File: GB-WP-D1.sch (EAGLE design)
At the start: 9 parts

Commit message: Add files via upload
WEMOS D1 mini size
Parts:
- removed JP2: (no value), pinhead_v2:PINHD-1X5/OCT
- removed JP5: (no value), pinhead_v2:PINHD-1X4/OCT
- added U$3: KAMENRIDER_LOGOV2_COLOR_OPAC, kamenrider:KAMENRIDER_LOGOV2_COLOR_OPAC
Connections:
- net 3.3V: no longer JP2.5, JP5.3
- net 5V: no longer JP2.4
- net D0: no longer JP2.1
- net D2: no longer JP5.1
- net D3: no longer JP2.2
- net GND: no longer JP2.3, JP5.4
- net N$7: no longer JP5.2
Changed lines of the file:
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@@
 <part name="JP4" library="pinhead_v2" deviceset="PINHD-1X6" device="/OCT"/>
 <part name="JP1" library="pinhead_v2" deviceset="PINHD-1X4" device="/OCT"/>
-<part name="JP5" library="pinhead_v2" deviceset="PINHD-1X4" device="/OCT"/>
 <part name="LED1" library="led" library_urn="urn:adsk.eagle:library:259" deviceset="LED" device="3MM" package3d_urn="urn:adsk.eagle:package:15797/1"/>
-<part name="JP2" library="pinhead_v2" deviceset="PINHD-1X5" device="/OCT"/>
 <part name="JP3" library="pinhead_v2" deviceset="PINHD-1X8" device="/OCT"/>
 <part name="JP6" library="pinhead_v2" deviceset="PINHD-1X8" device="/OCT"/>
+<part name="U$3" library="kamenrider" deviceset="KAMENRIDER_LOGO" device="V2_COLOR_OPAC"/>
 </parts>
 <sheets>
@@
 <attribute name="VALUE" x="153.67" y="55.88" size="1.778" layer="96"/>
 </instance>
-<instance part="JP5" gate="A" x="167.64" y="63.5" smashed="yes">
-<attribute name="NAME" x="161.29" y="71.755" size="1.778" layer="95"/>
-<attribute name="VALUE" x="161.29" y="55.88" size="1.778" layer="96"/>
-</instance>
 <instance part="LED1" gate="G$1" x="109.22" y="88.9" smashed="yes">
 <attribute name="NAME" x="112.776" y="84.328" size="1.778" layer="95" rot="R90"/>
 <attribute name="VALUE" x="114.935" y="84.328" size="1.778" layer="96" rot="R90"/>
 </instance>
-<instance part="JP2" gate="A" x="96.52" y="73.66" smashed="yes">
-<attribute name="NAME" x="90.17" y="81.915" size="1.778" layer="95"/>
-<attribute name="VALUE" x="90.17" y="63.5" size="1.778" layer="96"/>
-</instance>
 <instance part="JP3" gate="A" x="31.242" y="101.6" smashed="yes" rot="MR0">
 <attribute name="VALUE" x="47.752" y="86.36" size="1.778" layer="96" rot="MR0"/>
@@
 <attribute name="VALUE" x="227.33" y="88.9" size="1.778" layer="96" rot="MR0"/>
 </instance>
+<instance part="U$3" gate="G$1" x="86.36" y="7.62" smashed="yes"/>
 </instances>
 <busses>
@@
 <junction x="205.74" y="96.52"/>
 <wire x1="193.04" y1="96.52" x2="193.04" y2="60.96" width="0.1524" layer="91"/>
-<pinref part="JP5" gate="A" pin="4"/>
-<wire x1="193.04" y1="60.96" x2="165.1" y2="60.96" width="0.1524" layer="91"/>
+<wire x1="193.04" y1="60.96" x2="157.48" y2="60.96" width="0.1524" layer="91"/>
 <pinref part="JP1" gate="A" pin="4"/>
-<wire x1="157.48" y1="60.96" x2="165.1" y2="60.96" width="0.1524" layer="91"/>
 <pinref part="U$2" gate="G$1" pin="GND"/>
 <pinref part="JP4" gate="A" pin="6"/>
@@
 <wire x1="180.34" y1="78.74" x2="101.6" y2="78.74" width="0.1524" layer="91"/>
 <pinref part="JP6" gate="A" pin="7"/>
-<junction x="165.1" y="60.96"/>
 <wire x1="101.6" y1="78.74" x2="101.6" y2="73.66" width="0.1524" layer="91"/>
-<pinref part="JP2" gate="A" pin="3"/>
 <wire x1="101.6" y1="73.66" x2="93.98" y2="73.66" width="0.1524" layer="91"/>
 </segment>
@@
 <wire x1="223.52" y1="104.14" x2="187.96" y2="104.14" width="0.1524" layer="91"/>
 <wire x1="187.96" y1="104.14" x2="187.96" y2="68.58" width="0.1524" layer="91"/>
-<pinref part="JP5" gate="A" pin="1"/>
-<wire x1="187.96" y1="68.58" x2="165.1" y2="68.58" width="0.1524" layer="91"/>
+<wire x1="187.96" y1="68.58" x2="157.48" y2="68.58" width="0.1524" layer="91"/>
 <pinref part="JP1" gate="A" pin="1"/>
-<wire x1="165.1" y1="68.58" x2="157.48" y2="68.58" width="0.1524" layer="91"/>
 <pinref part="JP6" gate="A" pin="4"/>
-<junction x="165.1" y="68.58"/>
 </segment>
 </net>
@@
 <segment>
 <label x="40.64" y="106.68" size="1.778" layer="95"/>
-<pinref part="JP2" gate="A" pin="1"/>
-<wire x1="39.37" y1="106.68" x2="40.64" y2="106.68" width="0.1524" layer="91"/>
-<wire x1="40.64" y1="106.68" x2="93.98" y2="106.68" width="0.1524" layer="91"/>
+<wire x1="33.782" y1="106.68" x2="93.98" y2="106.68" width="0.1524" layer="91"/>
 <wire x1="93.98" y1="106.68" x2="93.98" y2="78.74" width="0.1524" layer="91"/>
 <pinref part="JP3" gate="A" pin="3"/>
-<wire x1="33.782" y1="106.68" x2="39.37" y2="106.68" width="0.1524" layer="91"/>
 </segment>
 </net>
@@
 <wire x1="223.52" y1="101.6" x2="182.88" y2="101.6" width="0.1524" layer="91"/>
 <wire x1="182.88" y1="101.6" x2="182.88" y2="76.2" width="0.1524" layer="91"/>
-<pinref part="JP2" gate="A" pin="2"/>
 <wire x1="182.88" y1="76.2" x2="93.98" y2="76.2" width="0.1524" layer="91"/>
 <pinref part="JP6" gate="A" pin="5"/>
@@
 <wire x1="215.9" y1="53.34" x2="99.06" y2="53.34" width="0.1524" layer="91"/>
 <wire x1="99.06" y1="53.34" x2="99.06" y2="71.12" width="0.1524" layer="91"/>
-<pinref part="JP2" gate="A" pin="4"/>
 <wire x1="99.06" y1="71.12" x2="93.98" y2="71.12" width="0.1524" layer="91"/>
 <pinref part="JP6" gate="A" pin="8"/>
@@
 <wire x1="127" y1="91.44" x2="172.72" y2="91.44" width="0.1524" layer="91"/>
 <wire x1="172.72" y1="91.44" x2="172.72" y2="63.5" width="0.1524" layer="91"/>
-<pinref part="JP5" gate="A" pin="3"/>
 <pinref part="JP1" gate="A" pin="3"/>
-<wire x1="157.48" y1="63.5" x2="165.1" y2="63.5" width="0.1524" layer="91"/>
-<wire x1="172.72" y1="63.5" x2="165.1" y2="63.5" width="0.1524" layer="91"/>
-<junction x="165.1" y="63.5"/>
-<pinref part="JP2" gate="A" pin="5"/>
+<wire x1="172.72" y1="63.5" x2="157.48" y2="63.5" width="0.1524" layer="91"/>
 <wire x1="53.34" y1="68.58" x2="93.98" y2="68.58" width="0.1524" layer="91"/>
 </segment>
@@
 <wire x1="223.52" y1="106.68" x2="185.42" y2="106.68" width="0.1524" layer="91"/>
 <wire x1="185.42" y1="106.68" x2="185.42" y2="66.04" width="0.1524" layer="91"/>
-<pinref part="JP5" gate="A" pin="2"/>
-<wire x1="185.42" y1="66.04" x2="165.1" y2="66.04" width="0.1524" layer="91"/>
+<wire x1="185.42" y1="66.04" x2="157.48" y2="66.04" width="0.1524" layer="91"/>
 <pinref part="JP1" gate="A" pin="2"/>
-<wire x1="165.1" y1="66.04" x2="157.48" y2="66.04" width="0.1524" layer="91"/>
 <pinref part="JP6" gate="A" pin="3"/>
-<junction x="165.1" y="66.04"/>
 </segment>
 </net>
@@
 </drawing>
 <compatibility>
+<note version="6.3" minversion="6.2.2" severity="warning">
+Since Version 6.2.2 text objects can contain more than one line,
+which will not be processed correctly with this version.
+</note>
 <note version="8.2" severity="warning">
 Since Version 8.2, EAGLE supports online libraries. The ids

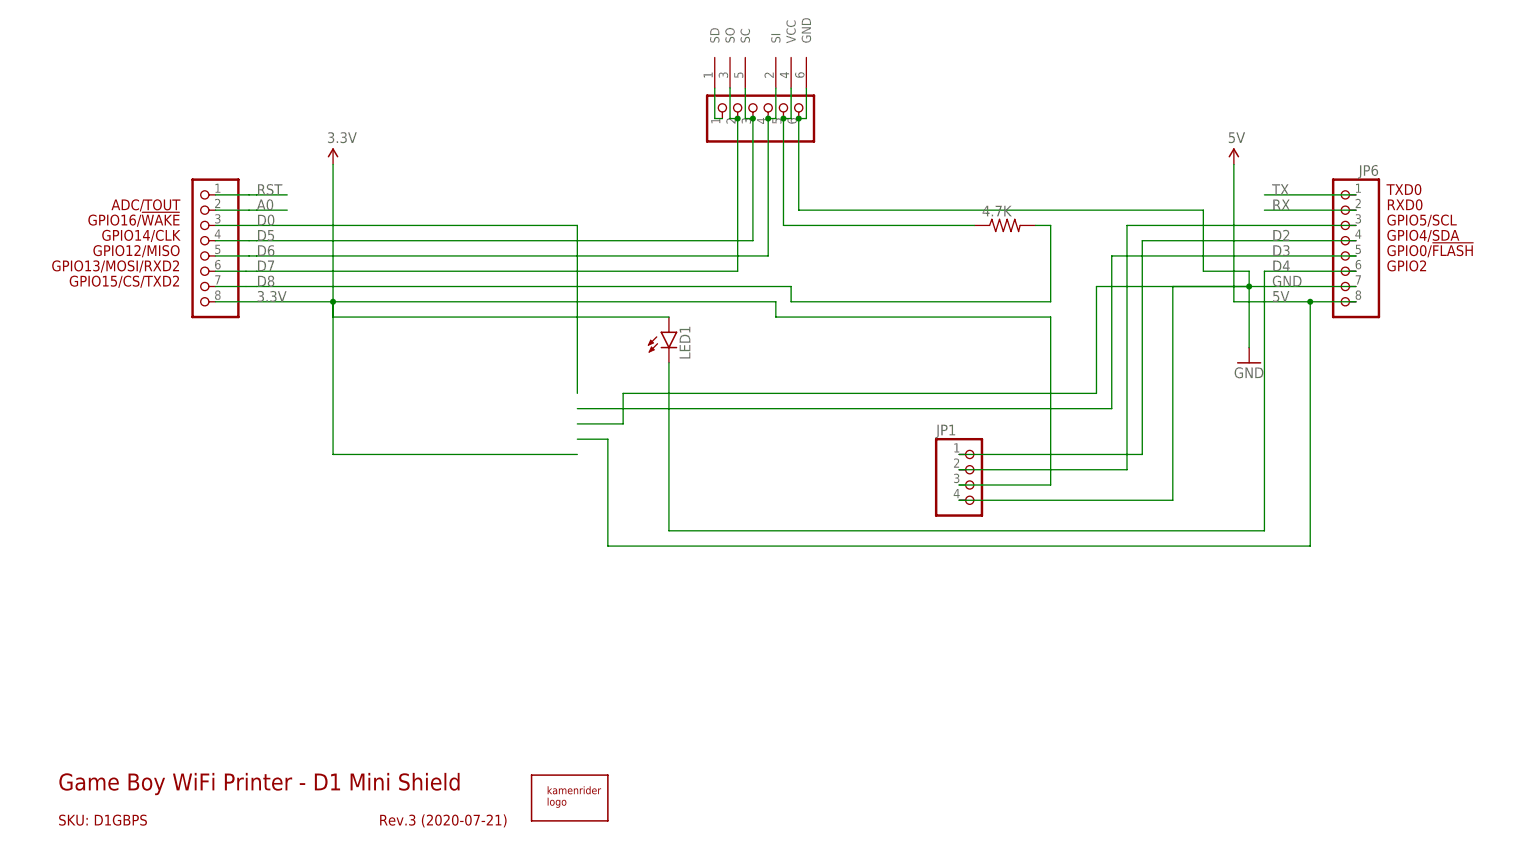
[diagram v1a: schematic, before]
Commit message: Add files via upload
Added optional SMD 1206 fotprint for resistor and LED
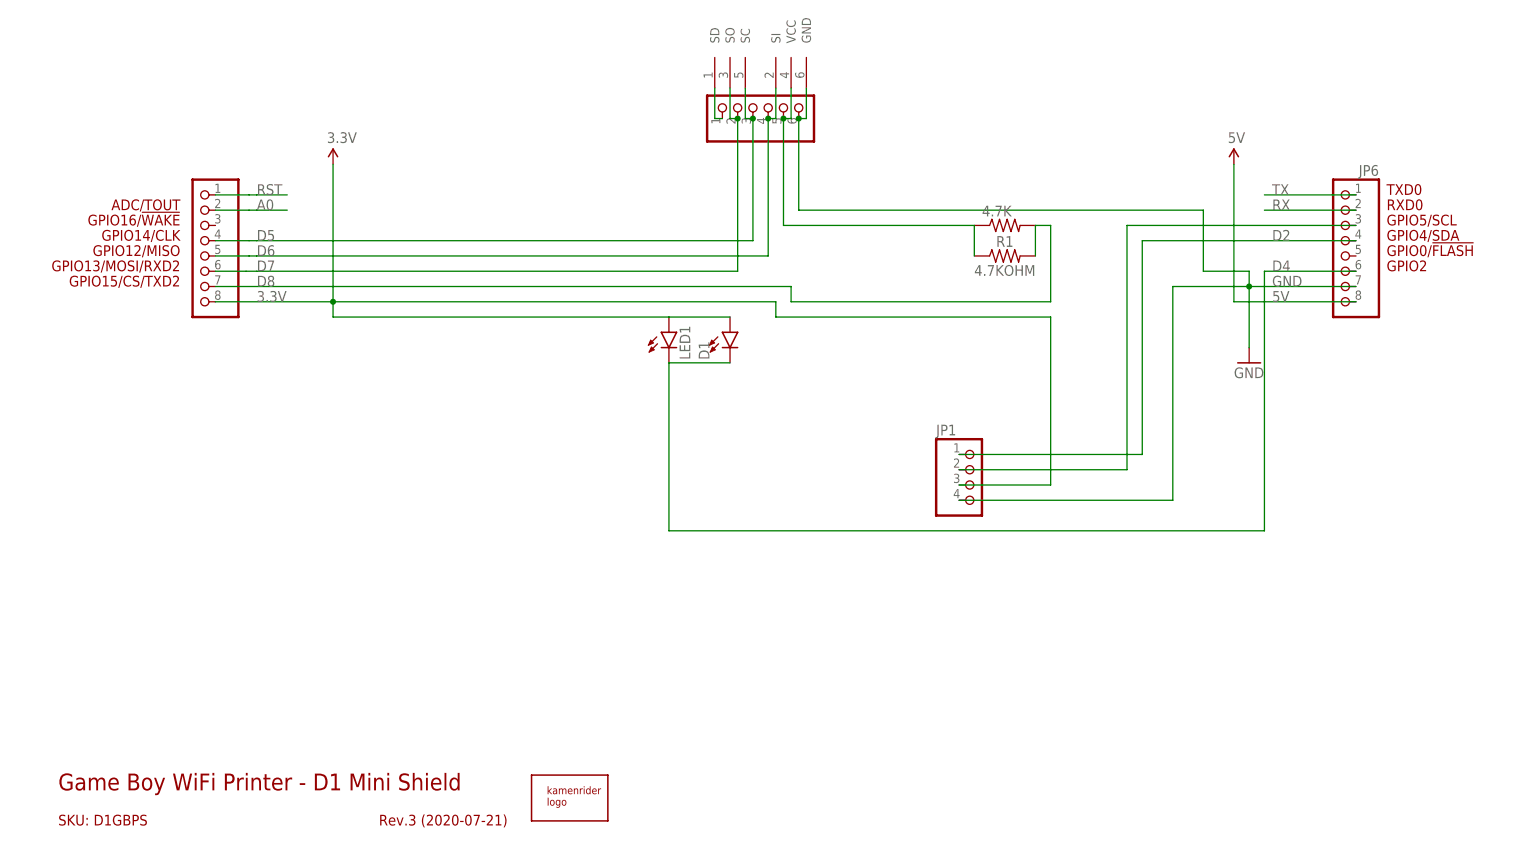
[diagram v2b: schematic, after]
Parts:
- added D1: (no value), SparkFun-LED:LED1206
- added R1: 4.7KOHM, SparkFun-Resistors:4.7KOHM
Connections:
- removed net D0: JP3.3
- removed net D3: JP6.5
- net 3.3V: now also D1.A
- net D4: now also D1.C
- net D8: now also R1.2
- net N$5: now also R1.1
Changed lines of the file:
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@@
 <part name="JP6" library="pinhead_v2" deviceset="PINHD-1X8" device="/OCT"/>
 <part name="U$3" library="kamenrider" deviceset="KAMENRIDER_LOGO" device="V2_COLOR_OPAC"/>
+<part name="D1" library="SparkFun-LED" deviceset="LED" device="1206"/>
+<part name="R1" library="SparkFun-Resistors" deviceset="4.7KOHM" device=""/>
 </parts>
 <sheets>
@@
 </instance>
 <instance part="U$3" gate="G$1" x="86.36" y="7.62" smashed="yes"/>
+<instance part="D1" gate="D1" x="119.38" y="88.9" smashed="yes">
+<attribute name="NAME" x="115.951" y="84.328" size="1.778" layer="95" font="vector" rot="R90"/>
+<attribute name="VALUE" x="121.285" y="84.328" size="1.778" layer="96" font="vector" rot="R90" align="top-left"/>
+</instance>
+<instance part="R1" gate="G$1" x="165.1" y="101.6" smashed="yes">
+<attribute name="NAME" x="165.1" y="103.124" size="1.778" layer="95" font="vector" align="bottom-center"/>
+<attribute name="VALUE" x="165.1" y="100.076" size="1.778" layer="96" font="vector" align="top-center"/>
+</instance>
 </instances>
 <busses>
@@
 <wire x1="198.12" y1="99.06" x2="205.74" y2="99.06" width="0.1524" layer="91"/>
 <wire x1="205.74" y1="99.06" x2="205.74" y2="96.52" width="0.1524" layer="91"/>
-<wire x1="205.74" y1="96.52" x2="180.34" y2="96.52" width="0.1524" layer="91"/>
-<wire x1="180.34" y1="96.52" x2="180.34" y2="78.74" width="0.1524" layer="91"/>
-<wire x1="180.34" y1="78.74" x2="101.6" y2="78.74" width="0.1524" layer="91"/>
 <pinref part="JP6" gate="A" pin="7"/>
-<wire x1="101.6" y1="78.74" x2="101.6" y2="73.66" width="0.1524" layer="91"/>
-<wire x1="101.6" y1="73.66" x2="93.98" y2="73.66" width="0.1524" layer="91"/>
 </segment>
 </net>
@@
 <segment>
 <label x="40.64" y="96.52" size="1.778" layer="95"/>
-<wire x1="38.862" y1="96.52" x2="40.64" y2="96.52" width="0.1524" layer="91"/>
-<wire x1="40.64" y1="96.52" x2="129.54" y2="96.52" width="0.1524" layer="91"/>
+<wire x1="33.782" y1="96.52" x2="129.54" y2="96.52" width="0.1524" layer="91"/>
 <wire x1="129.54" y1="96.52" x2="129.54" y2="93.98" width="0.1524" layer="91"/>
 <wire x1="129.54" y1="93.98" x2="172.72" y2="93.98" width="0.1524" layer="91"/>
@@
 <wire x1="172.72" y1="106.68" x2="170.18" y2="106.68" width="0.1524" layer="91"/>
 <pinref part="JP3" gate="A" pin="7"/>
-<wire x1="33.782" y1="96.52" x2="38.862" y2="96.52" width="0.1524" layer="91"/>
+<wire x1="170.18" y1="106.68" x2="170.18" y2="101.6" width="0.1524" layer="91"/>
+<pinref part="R1" gate="G$1" pin="2"/>
 </segment>
 </net>
@@
 <wire x1="40.64" y1="111.76" x2="45.72" y2="111.76" width="0.1524" layer="91"/>
 <wire x1="33.782" y1="111.76" x2="39.37" y2="111.76" width="0.1524" layer="91"/>
-</segment>
-</net>
-<net name="D0" class="0">
-<segment>
-<label x="40.64" y="106.68" size="1.778" layer="95"/>
-<wire x1="33.782" y1="106.68" x2="93.98" y2="106.68" width="0.1524" layer="91"/>
-<wire x1="93.98" y1="106.68" x2="93.98" y2="78.74" width="0.1524" layer="91"/>
-<pinref part="JP3" gate="A" pin="3"/>
 </segment>
 </net>
@@
 <pinref part="JP6" gate="A" pin="6"/>
 <wire x1="223.52" y1="99.06" x2="208.28" y2="99.06" width="0.1524" layer="91"/>
-</segment>
-</net>
-<net name="D3" class="0">
-<segment>
-<label x="209.55" y="101.6" size="1.778" layer="95"/>
-<wire x1="223.52" y1="101.6" x2="182.88" y2="101.6" width="0.1524" layer="91"/>
-<wire x1="182.88" y1="101.6" x2="182.88" y2="76.2" width="0.1524" layer="91"/>
-<wire x1="182.88" y1="76.2" x2="93.98" y2="76.2" width="0.1524" layer="91"/>
-<pinref part="JP6" gate="A" pin="5"/>
+<wire x1="109.22" y1="83.82" x2="119.38" y2="83.82" width="0.1524" layer="91"/>
+<pinref part="D1" gate="D1" pin="C"/>
 </segment>
 </net>
@@
 <segment>
 <label x="209.55" y="93.98" size="1.778" layer="95"/>
-<wire x1="215.9" y1="93.98" x2="203.2" y2="93.98" width="0.1524" layer="91"/>
+<wire x1="223.52" y1="93.98" x2="203.2" y2="93.98" width="0.1524" layer="91"/>
 <pinref part="U$1" gate="G$1" pin="5V"/>
 <wire x1="203.2" y1="116.84" x2="203.2" y2="93.98" width="0.1524" layer="91"/>
-<wire x1="215.9" y1="93.98" x2="215.9" y2="53.34" width="0.1524" layer="91"/>
-<wire x1="215.9" y1="53.34" x2="99.06" y2="53.34" width="0.1524" layer="91"/>
-<wire x1="99.06" y1="53.34" x2="99.06" y2="71.12" width="0.1524" layer="91"/>
-<wire x1="99.06" y1="71.12" x2="93.98" y2="71.12" width="0.1524" layer="91"/>
 <pinref part="JP6" gate="A" pin="8"/>
-<wire x1="223.52" y1="93.98" x2="215.9" y2="93.98" width="0.1524" layer="91"/>
-<junction x="215.9" y="93.98"/>
 </segment>
 </net>
@@
 <wire x1="53.34" y1="91.44" x2="109.22" y2="91.44" width="0.1524" layer="91"/>
 <junction x="53.34" y="93.98"/>
-<wire x1="53.34" y1="93.98" x2="53.34" y2="68.58" width="0.1524" layer="91"/>
 <pinref part="JP3" gate="A" pin="8"/>
 <wire x1="53.34" y1="93.98" x2="127" y2="93.98" width="0.1524" layer="91"/>
@@
 <pinref part="JP1" gate="A" pin="3"/>
 <wire x1="172.72" y1="63.5" x2="157.48" y2="63.5" width="0.1524" layer="91"/>
-<wire x1="53.34" y1="68.58" x2="93.98" y2="68.58" width="0.1524" layer="91"/>
+<wire x1="109.22" y1="91.44" x2="119.38" y2="91.44" width="0.1524" layer="91"/>
+<pinref part="D1" gate="D1" pin="A"/>
 </segment>
 </net>
@@
 <wire x1="128.27" y1="106.68" x2="160.02" y2="106.68" width="0.1524" layer="91"/>
 <junction x="128.27" y="124.46"/>
-</segment>
-</net>
+<wire x1="160.02" y1="106.68" x2="160.02" y2="101.6" width="0.1524" layer="91"/>
+<pinref part="R1" gate="G$1" pin="1"/>
+</segment>
+</net>
